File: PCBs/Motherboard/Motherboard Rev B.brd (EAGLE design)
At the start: 95.9 x 90.2 mm, 56 parts, among them J2 MOLEX_504050-0491, Q1 16MHz, U1 Value, X1 2514-5

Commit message: Use 5-pin Pico-Lock for sensor harness
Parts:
- removed J2: MOLEX_504050-0491, Molex 504050-0491:MOLEX_5040500491
- added J1: MOLEX_504050-0591, Molex 504050:MOLEX_5040500591
- moved C18 4.02 mm to (66.2, 48.1)
- moved C17 0.64 mm to (67.6, 50.8)
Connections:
- new net TEMP_RET: J1.3
- net 3V: now also J1.1, J1.4; no longer J2.1, J2.3
- net SHIELD: now also J1.SH1, J1.SH2; no longer J2.SH1, J2.SH2
- net STRN: now also J1.5; no longer J2.4, R12.2, R17.1
- net TEMP: now also J1.2, R12.2, R17.1; no longer J2.2
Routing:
- net N$12: track 7.39 -> 13.0 mm
- net GND: track 43.1 -> 47.6 mm, vias 18 -> 20
- net N$4: track 9.64 -> 13.8 mm

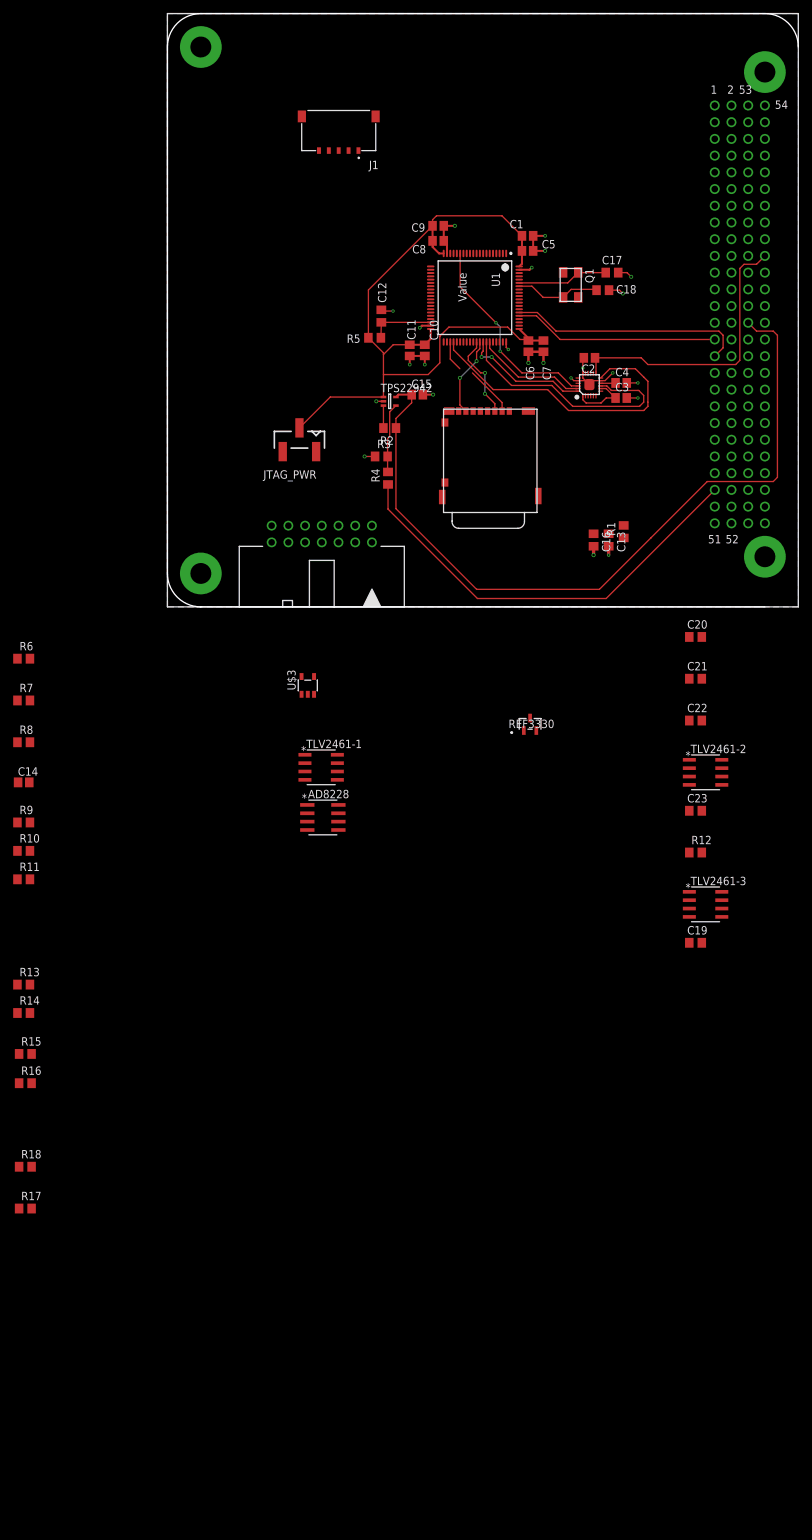
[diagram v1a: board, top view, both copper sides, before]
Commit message: Changed opamps used in sensing circuits
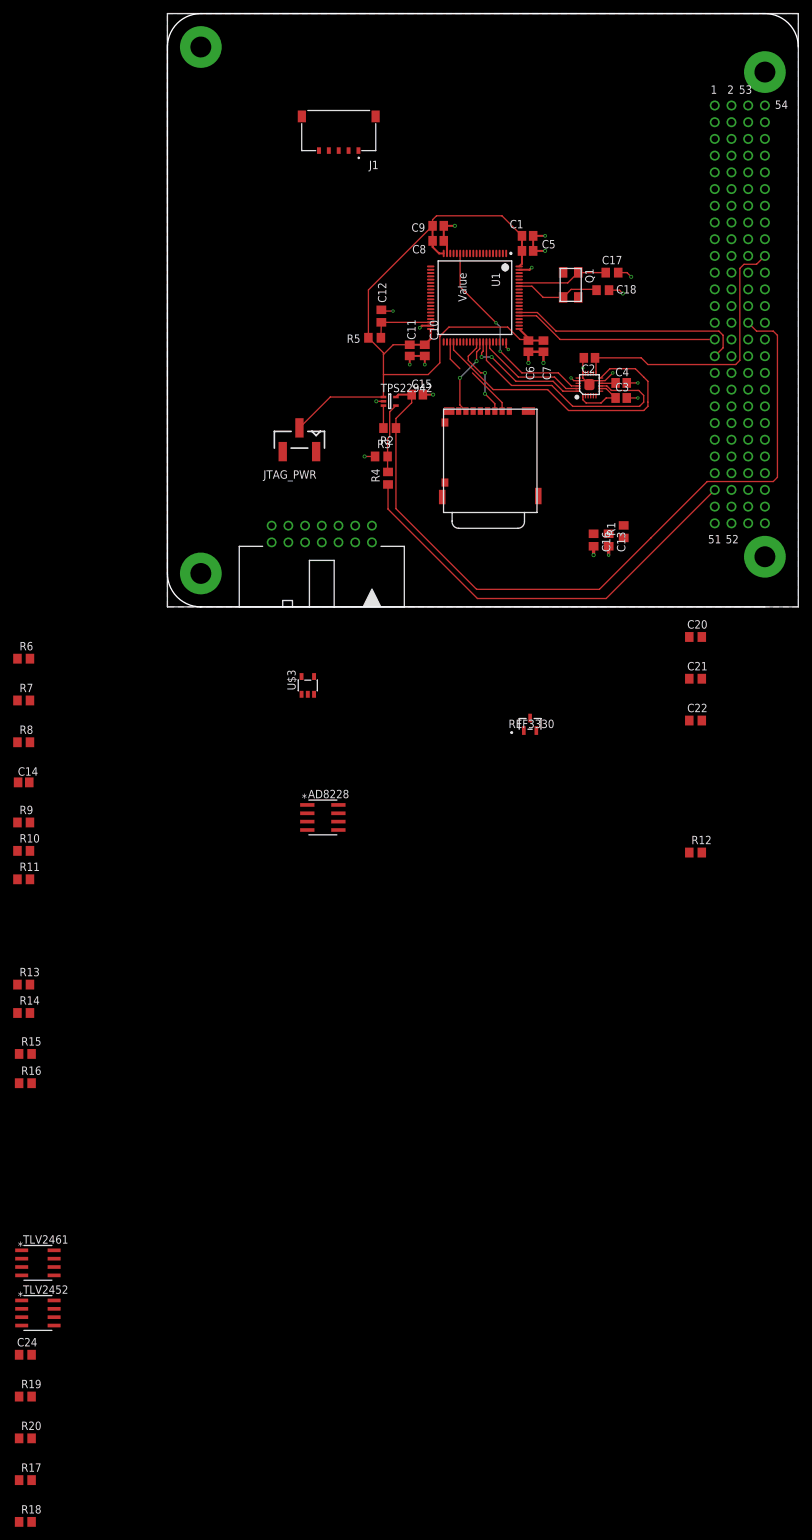
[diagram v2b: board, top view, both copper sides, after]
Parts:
- removed C19, C23: 0.1uF, resistor:C0805
- removed TLV2461-1, TLV2461-2, TLV2461-3: TLV2461A_D_8, TLV2461:D8
- added C24: 0.1uF, resistor:C0805
- added R19, R20: 0, resistor:R0805
- added TLV2452: TLV2452, TLV24xx:D8
- added TLV2461: TLV2461A_D_8, TLV24xx:D8
- R17, R18: value 0 -> 10k
- moved R18 54.0 mm to (-21.6, -139.1)
- moved R17 41.3 mm to (-21.6, -132.7)
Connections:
- removed net N$13: R17.2, TLV2461-3.3
- removed net N$14: AD8228.1, AD8228.7, R10.2, R11.1, R15.1, TLV2461-2.3
- removed net N$16: R18.1, TLV2461-3.2, TLV2461-3.6
- removed net N$9: AD8228.6, TLV2461-2.2, TLV2461-2.6
- new net 1V5: AD8228.6, TLV2452.1, TLV2452.2
- new net 1V5_REF: R17.1, R18.2, TLV2452.3
- new net N$15: R19.1, TLV2452.6, TLV2452.7
- new net N$17: R20.1, TLV2452.5
- net 3V: now also R17.2, TLV2461.2, TLV2461.6; no longer TLV2461-1.2, TLV2461-1.6
- net 3V_REF: now also TLV2461.3; no longer TLV2461-1.3
- net GND: now also C24.2, R18.1, TLV2452.4, TLV2461.4; no longer C19.2, C23.2, TLV2461-1.4, TLV2461-2.4
- net N$10: now also AD8228.1, AD8228.7, R10.2, R11.1, R15.1; no longer TLV2461-3.4
- net STRAIN_OUT: no longer R18.2
- net SW10: now also C24.1, TLV2452.8, TLV2461.7; no longer C19.1, C23.1, TLV2461-1.7, TLV2461-2.7, TLV2461-3.7
- net TEMP: now also R20.2; no longer R17.1
- net TEMP_OUT: now also R19.2

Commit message: Add xtals, antenna harness, finish most wiring
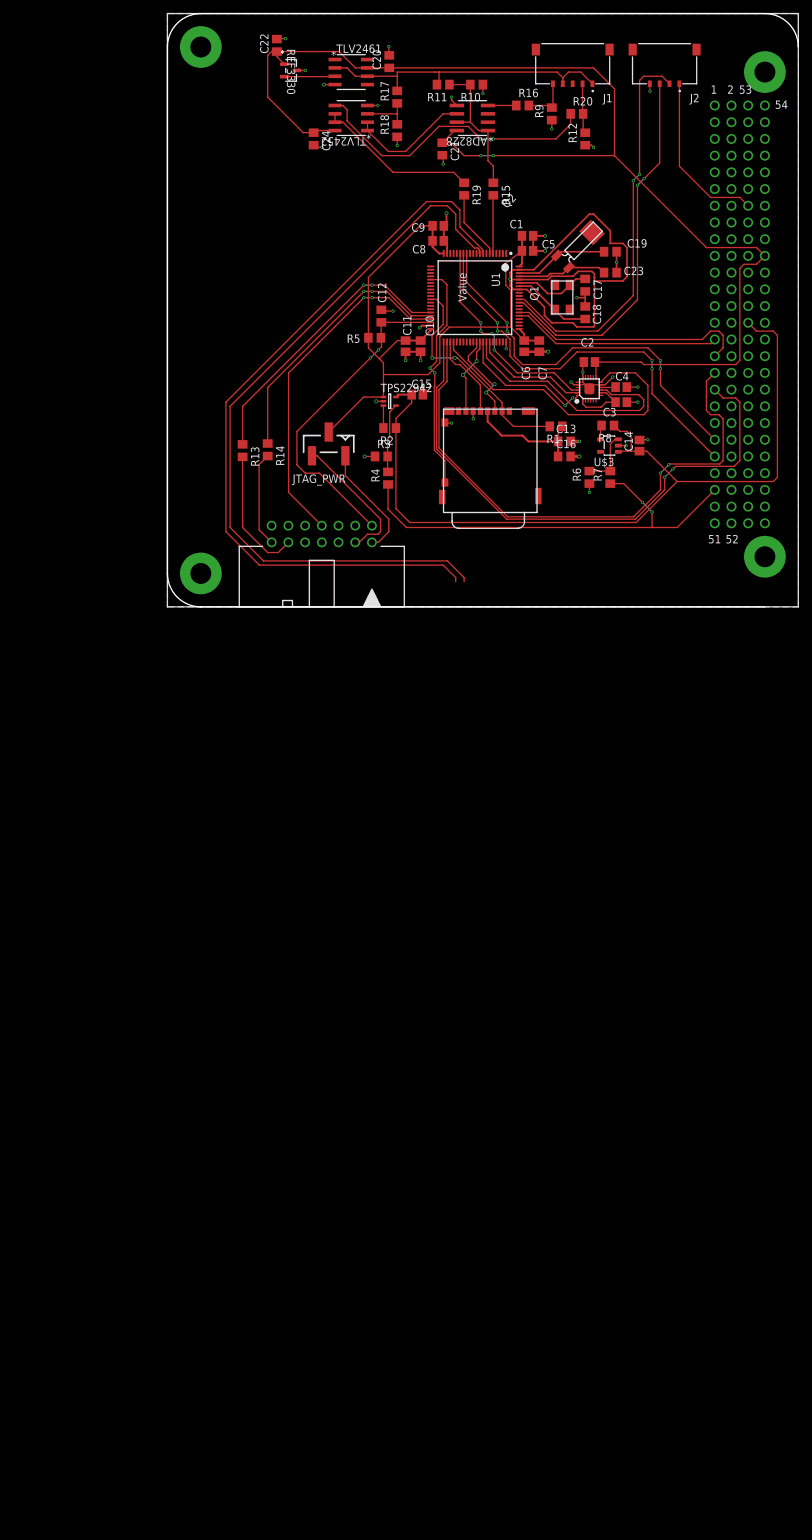
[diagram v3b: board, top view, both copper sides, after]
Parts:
- added C19, C23: 12pF, resistor:C0805
- added J2: MOLEX_504050-0491, Molex 504050-0491:MOLEX_5040500491
- added Q2: 32.768k, MS1V-T1K:MS1V-T1K
- Q1: value 16MHz -> 16M
- moved R18 218.9 mm to (34.9, 72.4), turned to 90 degrees
- moved R20 218.0 mm to (62.2, 74.9)
- moved R17 217.7 mm to (34.9, 77.5), turned to 90 degrees
- moved R19 195.3 mm to (45.1, 63.5), turned to 270 degrees
- moved C24 189.9 mm to (22.2, 71.1), turned to 270 degrees
- moved TLV2452 187.8 mm to (27.9, 74.3), turned to 180 degrees
- moved TLV2461 187.1 mm to (27.9, 81.3)
- moved R16 166.7 mm to (54.0, 76.2)
- moved R15 149.5 mm to (49.5, 63.5), turned to 270 degrees
- moved R11 136.6 mm to (41.9, 79.4), turned to 180 degrees
- moved R10 135.3 mm to (47.0, 79.4), turned to 180 degrees
- moved R9 134.3 mm to (58.4, 74.9), turned to 90 degrees
- moved C22 120.7 mm to (16.6, 85.3), turned to 90 degrees
- moved R12 109.7 mm to (63.5, 71.1), turned to 90 degrees
- moved AD8228 108.7 mm to (46.4, 74.3), turned to 180 degrees
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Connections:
- removed net 3V1: C14.1
- new net N$13: C19.1, Q2.2, U1.78
- new net N$9: C23.1, Q2.1, U1.77
- net 3V3: now also C14.1; no longer AD8228.8, C21.1
- net AGND: now also C17.2, C18.2, C19.2, C23.2
- net GND: now also J2.4; no longer C17.2, C18.2
- net SCL_ANT: now also J2.2
- net SDA_ANT: now also J2.3
- net SHIELD: now also J2.SH1, J2.SH2
- net SW10: now also AD8228.8, C21.1
- net SW5: now also J2.1
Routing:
- net SW10: track 52.7 -> 198.4 mm, vias 0 -> 2
- net EXT_RXD: track 0.00 -> 114.9 mm
- net EXT_TXD: track 0.00 -> 113.0 mm
- net PINAVL1_RX: track 0.00 -> 85.5 mm, vias 0 -> 2
- net PINAVL1_TX: track 0.00 -> 84.8 mm, vias 0 -> 2
- net AGND: track 8.63 -> 87.7 mm, vias 3 -> 5
- net SCL_EPS: track 0.00 -> 61.5 mm, vias 0 -> 4
- net SCL_ANT: track 0.00 -> 60.0 mm, vias 0 -> 2
- net SDA_EPS: track 0.00 -> 58.7 mm, vias 0 -> 4
- net SDA_ANT: track 0.00 -> 56.5 mm, vias 0 -> 2
- net SBWTCK: track 0.00 -> 53.0 mm, vias 0 -> 2
- net 3V: track 0.00 -> 46.9 mm
- net N$17: track 0.00 -> 45.1 mm, vias 0 -> 2
- net JTAG_RXD: track 0.00 -> 43.7 mm, vias 0 -> 2
- net JTAG_TXD: track 0.00 -> 40.9 mm, vias 0 -> 2
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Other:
- board text added: "Ext UART and RBF here"

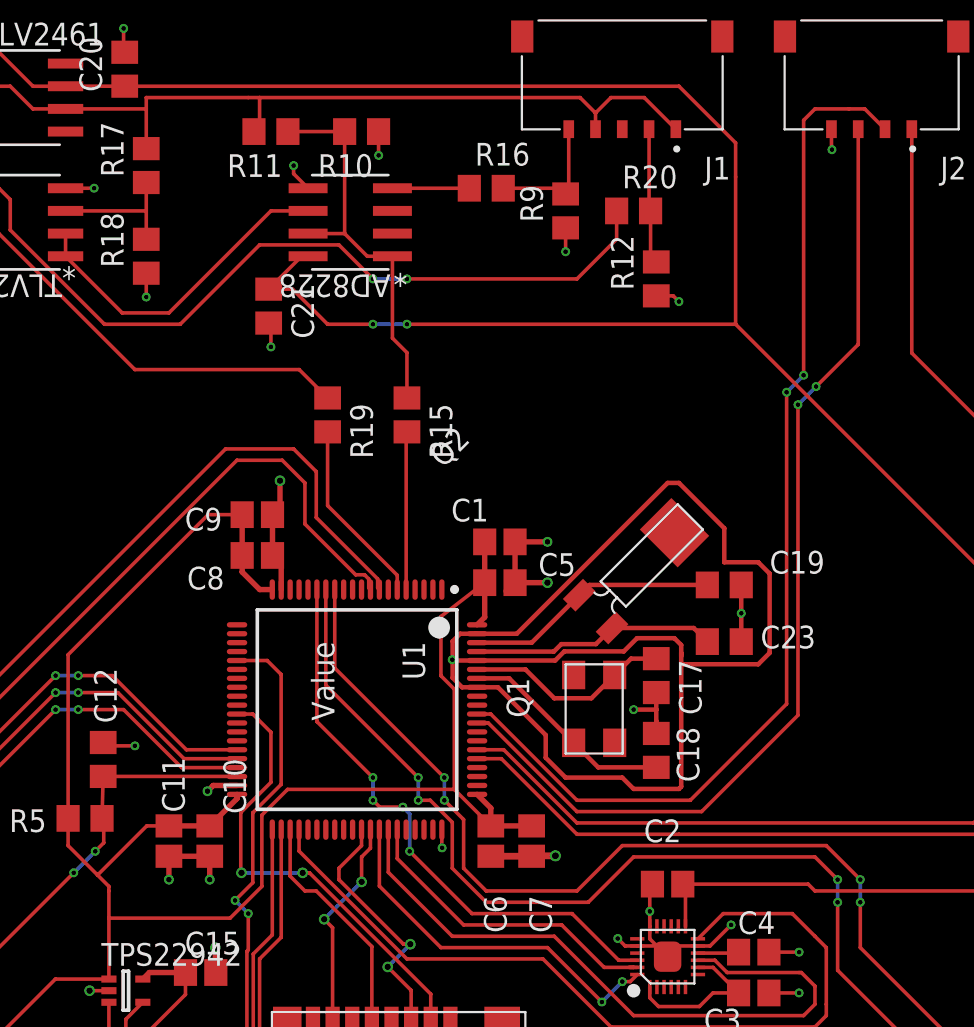
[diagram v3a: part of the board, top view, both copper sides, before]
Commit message: Add I2C pullups
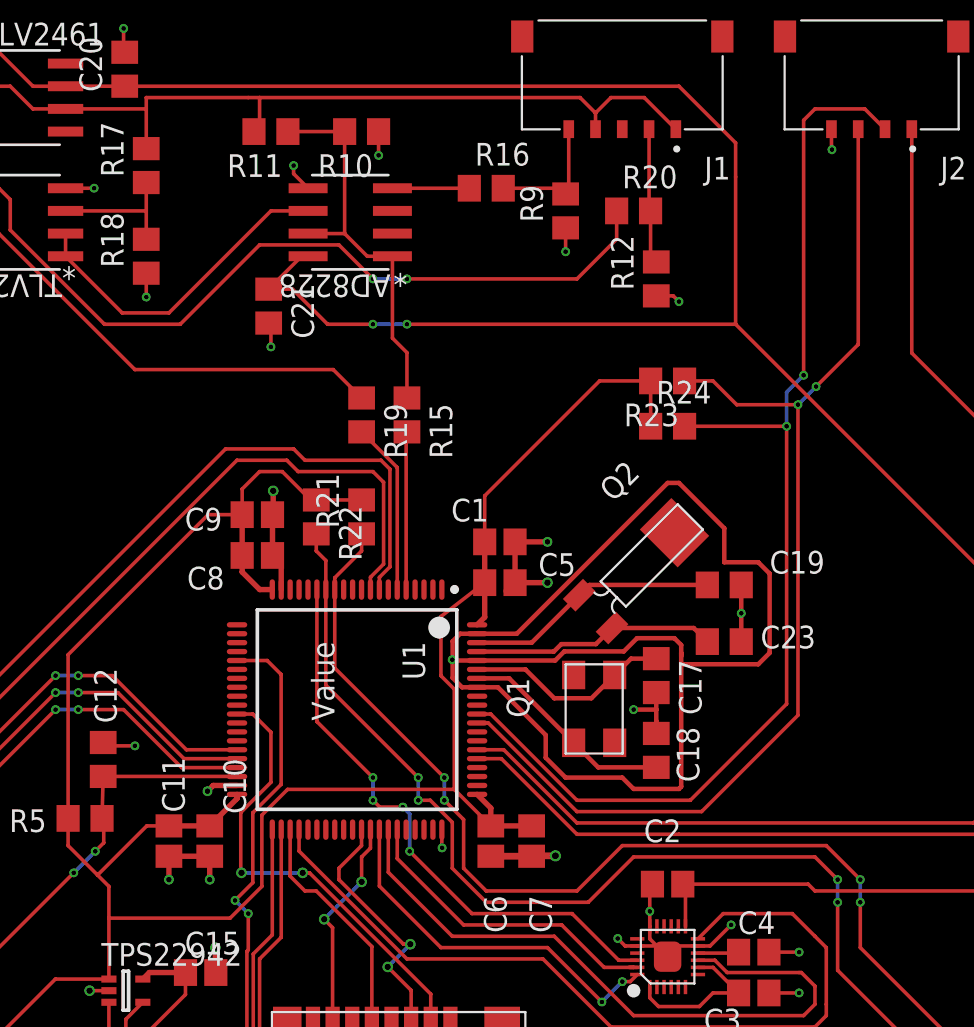
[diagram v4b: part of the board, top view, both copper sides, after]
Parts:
- added R21, R22, R23, R24: 10k, resistor:R0805
- moved R19 1.91 mm to (47.0, 63.5)
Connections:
- net 3V3_UC: now also R21.2, R22.1, R23.2, R24.1
- net SCL_ANT: now also R24.2
- net SCL_EPS: now also R22.2
- net SDA_ANT: now also R23.1
- net SDA_EPS: now also R21.1
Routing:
- net 3V3_UC: track 108.0 -> 134.3 mm
- net SDA_ANT: track 56.5 -> 63.4 mm
- net SCL_ANT: track 60.0 -> 65.7 mm
- net SDA_EPS: track 58.7 -> 62.4 mm
- net SCL_EPS: track 61.5 -> 64.8 mm
- net EXT_RXD: track 114.9 -> 117.9 mm
- net EXT_TXD: track 113.0 -> 115.9 mm
- net N$15: track 24.7 -> 26.6 mm
- net TEMP_OUT: track 10.5 -> 9.66 mm
- net GND: track 65.3 -> 64.6 mm

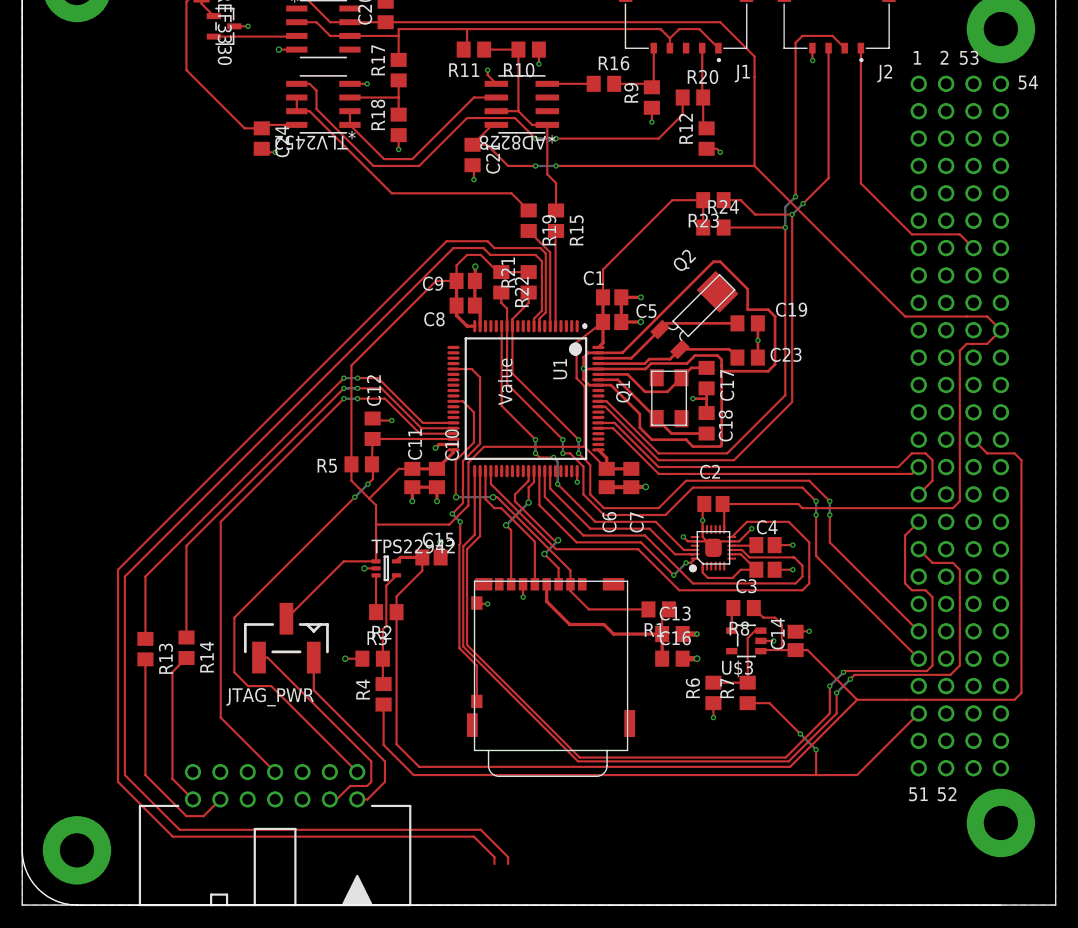
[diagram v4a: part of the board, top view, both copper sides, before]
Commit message: Move SD, make room for RBF
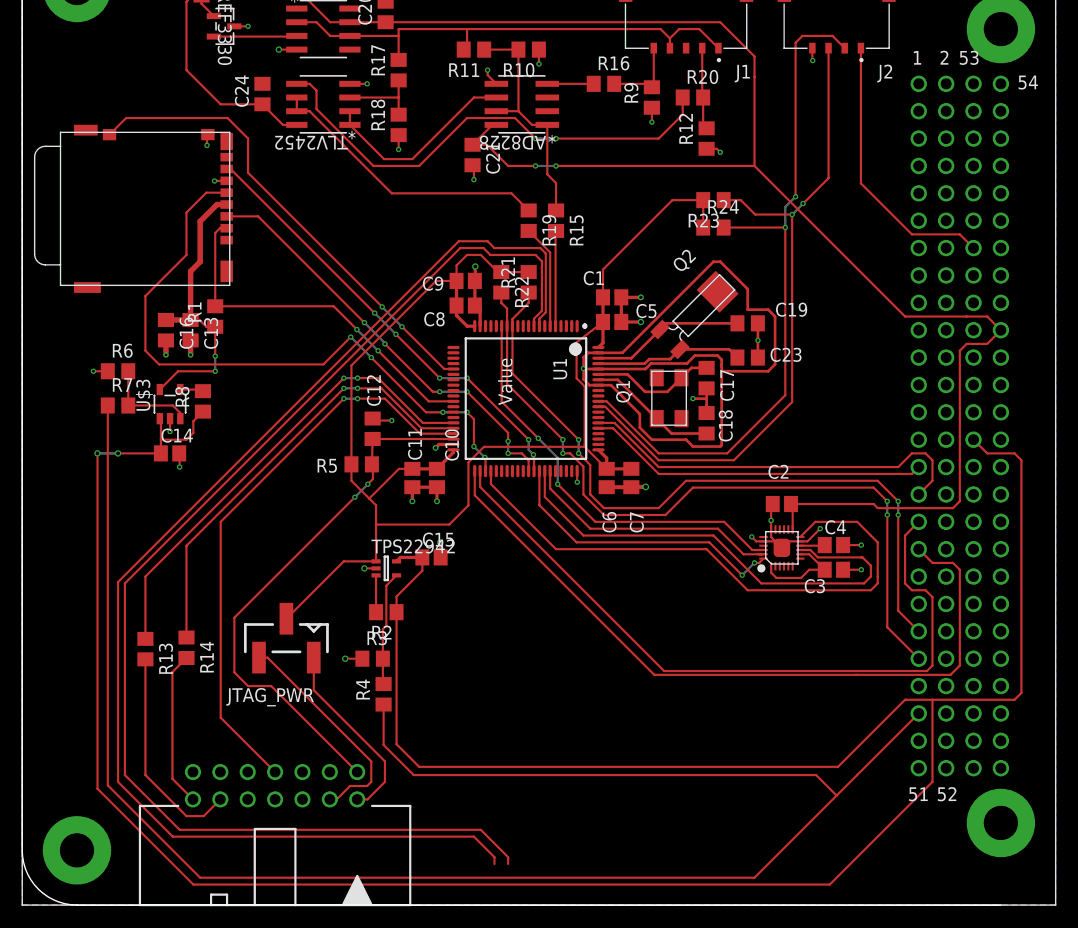
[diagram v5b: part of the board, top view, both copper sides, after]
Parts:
- moved R7 64.2 mm to (8.89, 46.4), turned to 0 degrees
- moved R6 62.8 mm to (8.89, 49.5), turned to 0 degrees
- moved C14 60.6 mm to (13.7, 41.9), turned to 0 degrees
- moved U$3 57.8 mm to (13.7, 46.5), turned to 0 degrees
- moved C16 56.0 mm to (13.3, 53.3), turned to 270 degrees
- moved R8 53.7 mm to (16.8, 46.7), turned to 90 degrees
- moved C13 52.9 mm to (15.6, 53.3), turned to 270 degrees
- moved R1 49.3 mm to (17.9, 54.6), turned to 90 degrees
- moved SD_CONN 45.7 mm to (19.6, 56.8), turned to 90 degrees
- moved C3 6.35 mm to (75.3, 31.1)
- moved C4 6.35 mm to (75.3, 33.4)
- moved C2 6.35 mm to (70.5, 37.2)
- moved U$2 6.35 mm to (70.5, 33.1)
- moved C24 4.13 mm to (22.3, 75.2), turned to 90 degrees
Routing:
- net 3V3: track 125.9 -> 248.0 mm, vias 0 -> 2
- net LI_OA_RESET: track 67.4 -> 168.1 mm, vias 2 -> 0
- net CLK_SD: track 12.8 -> 59.4 mm, vias 0 -> 6
- net MISO_SD: track 11.8 -> 41.5 mm, vias 2 -> 6
- net MOSI_SD: track 14.0 -> 39.6 mm, vias 2 -> 6
- net PINAVL1_TX: track 84.8 -> 66.4 mm, vias 2 -> 0
- net PINAVL1_RX: track 85.5 -> 68.2 mm, vias 2 -> 0
- net 3V3_SD: track 18.4 -> 27.4 mm, vias 0 -> 2
- net SD_DETECT: track 35.0 -> 44.1 mm
- net SW10: track 198.4 -> 191.8 mm
- net MOSI_IMU: track 20.9 -> 27.3 mm
- net CLK_IMU: track 17.8 -> 24.2 mm
- net MISO_IMU: track 38.1 -> 44.4 mm
- net INT_IMU: track 47.5 -> 53.8 mm
- net CS_IMU: track 32.9 -> 38.4 mm, vias 4 -> 2
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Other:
- board text added: "Ext UART, 5V, and RBF here"
- board text removed: "Ext UART and RBF here"
